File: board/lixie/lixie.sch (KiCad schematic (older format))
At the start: 27 parts

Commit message: got basic tokenizer working
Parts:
- added LS?: Speaker, symbol Speaker
- added R?: 10k, symbol R
- added R?: R, symbol R
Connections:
- net labels added: BOOT0, BTN_SLEEP, DBG_TCK, DBG_TMS, NRST, PIEZO
- wire segments 122 -> 131
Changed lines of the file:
@@
 	4900 9400 4600 9400
 Connection ~ 4600 9400
+Wire Wire Line
+	6250 9750 6600 9750
+Wire Wire Line
+	6250 9650 6600 9650
+Text Label 6600 9650 0    60   ~ 0
+DBG_TMS
+Text Label 6600 9750 0    60   ~ 0
+DBG_TCK
+Wire Wire Line
+	3650 9900 4900 9900
+Wire Wire Line
+	3650 10000 4900 10000
+Text Label 3650 9900 2    60   ~ 0
+NRST
+$Comp
+L R R?
+U 1 1 5E214C5B
+P 3850 10200
+F 0 "R?" V 3930 10200 50  0000 C CNN
+F 1 "10k" V 3850 10200 50  0000 C CNN
+F 2 "" V 3780 10200 50  0000 C CNN
+F 3 "" H 3850 10200 50  0000 C CNN
+	1    3850 10200
+	1    0    0    -1
+$EndComp
+Wire Wire Line
+	3850 10000 3850 10050
+Connection ~ 3850 10000
+$Comp
+L GND #PWR?
+U 1 1 5E21555C
+P 3850 10400
+F 0 "#PWR?" H 3850 10150 50  0001 C CNN
+F 1 "GND" H 3850 10250 50  0000 C CNN
+F 2 "" H 3850 10400 50  0001 C CNN
+F 3 "" H 3850 10400 50  0001 C CNN
+	1    3850 10400
+	1    0    0    -1
+$EndComp
+Wire Wire Line
+	3850 10350 3850 10400
+Text Label 3650 10000 2    60   ~ 0
+BOOT0
+Wire Wire Line
+	4900 11500 4600 11500
+Text Label 4600 11500 2    60   ~ 0
+BTN_SLEEP
+Wire Wire Line
+	3950 11400 4900 11400
+$Comp
+L Speaker LS?
+U 1 1 5E218279
+P 3550 11200
+F 0 "LS?" H 3600 11425 50  0000 R CNN
+F 1 "Speaker" H 3600 11350 50  0000 R CNN
+F 2 "" H 3550 11000 50  0000 C CNN
+F 3 "" H 3540 11150 50  0000 C CNN
+	1    3550 11200
+	0    -1   -1   0
+$EndComp
+$Comp
+L R R?
+U 1 1 5E218871
+P 3800 11400
+F 0 "R?" V 3880 11400 50  0000 C CNN
+F 1 "R" V 3800 11400 50  0000 C CNN
+F 2 "" V 3730 11400 50  0000 C CNN
+F 3 "" H 3800 11400 50  0000 C CNN
+	1    3800 11400
+	0    1    1    0
+$EndComp
+$Comp
+L GND #PWR?
+U 1 1 5E219525
+P 3550 11500
+F 0 "#PWR?" H 3550 11250 50  0001 C CNN
+F 1 "GND" H 3550 11350 50  0000 C CNN
+F 2 "" H 3550 11500 50  0001 C CNN
+F 3 "" H 3550 11500 50  0001 C CNN
+	1    3550 11500
+	1    0    0    -1
+$EndComp
+Wire Wire Line
+	3550 11400 3550 11500
+Text Label 4600 11400 2    60   ~ 0
+PIEZO
 $EndSCHEMATC

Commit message: made some footprints, fixed the power diode circuitry
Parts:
- removed Q?: Q_PJFET_DGS, symbol Q_PJFET_DGS
- removed R?: R, symbol R
- removed U?: LM66100, symbol LM66100
- added D?: D, symbol D
- added U?: MAX40200, symbol MAX40200
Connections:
- wire segments 131 -> 126
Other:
- note added: "3.3v Regulator"
- note added: "Ideal Diode"
- note added: "LED Matrix Driver"
- note added: "Main MCU"
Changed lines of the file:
@@
-$EndComp
-$Comp
-L LM66100 U?
-U 1 1 5E1F1034
-P 10450 9550
-F 0 "U?" H 10450 9600 60  0000 C CNN
-F 1 "LM66100" H 10450 9500 60  0000 C CNN
-F 2 "" H 10450 9400 60  0001 C CNN
-F 3 "" H 10450 9400 60  0001 C CNN
-	1    10450 9550
-	1    0    0    -1
 $EndComp
 $Comp
@@
 $EndComp
 $Comp
-L Q_PJFET_DGS Q?
-U 1 1 5E1F2946
-P 10450 10300
-F 0 "Q?" H 10650 10350 50  0000 L CNN
-F 1 "Q_PJFET_DGS" H 10650 10250 50  0000 L CNN
-F 2 "" H 10650 10400 50  0000 C CNN
-F 3 "" H 10450 10300 50  0000 C CNN
-	1    10450 10300
-	0    1    1    0
-$EndComp
-$Comp
-L R R?
-U 1 1 5E1F363E
-P 11400 9950
-F 0 "R?" V 11480 9950 50  0000 C CNN
-F 1 "R" V 11400 9950 50  0000 C CNN
-F 2 "" V 11330 9950 50  0000 C CNN
-F 3 "" H 11400 9950 50  0000 C CNN
-	1    11400 9950
-	1    0    0    -1
-$EndComp
-$Comp
-L +BATT #PWR?
-U 1 1 5E1F37C6
-P 11400 9750
-F 0 "#PWR?" H 11400 9600 50  0001 C CNN
-F 1 "+BATT" H 11400 9890 50  0000 C CNN
-F 2 "" H 11400 9750 50  0001 C CNN
-F 3 "" H 11400 9750 50  0001 C CNN
-	1    11400 9750
-	1    0    0    -1
-$EndComp
-$Comp
 L LED_ARGB D?
 U 1 1 5E1FE9E8
@@
 Connection ~ 6650 6250
 Wire Wire Line
-	9500 9300 9500 9200
-Wire Wire Line
-	11750 9100 11750 10400
-Wire Wire Line
-	11400 9750 11400 9800
-Connection ~ 11250 10100
+	9500 9200 9500 9550
 Connection ~ 11750 9300
 Wire Wire Line
-	11750 10400 10650 10400
-Connection ~ 9500 10100
-Wire Wire Line
-	10250 10100 9500 10100
-Wire Wire Line
-	10250 10100 10250 10400
-Wire Wire Line
-	10450 10100 11400 10100
-Wire Wire Line
-	11250 9550 11250 10100
-Wire Wire Line
-	11150 9550 11250 9550
-Wire Wire Line
 	9500 9550 9750 9550
-Wire Wire Line
-	9500 10300 9500 9550
 Wire Wire Line
 	9650 9800 9650 9850
@@
 Text Label 4600 11400 2    60   ~ 0
 PIEZO
+$Comp
+L MAX40200 U?
+U 1 1 5E374A62
+P 10450 9550
+F 0 "U?" H 10450 9600 60  0000 C CNN
+F 1 "MAX40200" H 10450 9500 60  0000 C CNN
+F 2 "" H 10450 9400 60  0001 C CNN
+F 3 "" H 10450 9400 60  0001 C CNN
+	1    10450 9550
+	1    0    0    -1
+$EndComp
+Wire Wire Line
+	9500 10100 9500 10300
+Connection ~ 9500 9300
+Wire Wire Line
+	11750 10100 11750 9300
+$Comp
+L D D?
+U 1 1 5E37A215
+P 10450 10100
+F 0 "D?" H 10450 10200 50  0000 C CNN
+F 1 "D" H 10450 10000 50  0000 C CNN
+F 2 "" H 10450 10100 50  0000 C CNN
+F 3 "" H 10450 10100 50  0000 C CNN
+	1    10450 10100
+	-1   0    0    1
+$EndComp
+Wire Wire Line
+	9500 10100 10300 10100
+Wire Wire Line
+	10600 10100 11750 10100
+Text Notes 10200 9150 0    60   ~ 0
+Ideal Diode
+Text Notes 12550 9150 0    60   ~ 0
+3.3v Regulator
+Text Notes 4700 3800 0    60   ~ 0
+LED Matrix Driver
+Text Notes 5350 8200 0    60   ~ 0
+Main MCU
 $EndSCHEMATC

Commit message: started working on layout
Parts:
- removed P?: USB_A, symbol USB_A
- added P1: USB_OTG, lixie:USB_Micro-B_Molex-105017-0001, symbol USB_OTG
- BT1: renamed from BT?; footprint (none) -> Pin_Headers:Pin_Header_Straight_1x02
- D1, D10, D11, D12, D13, D14, D15, D16, D2, D3, D4, D5, D6, D7, D8, D9: renamed from D?; footprint (none) -> lixie:LED_ARGB_0606
- D17: renamed from D?; footprint (none) -> Diodes_SMD:SOD-123
- LS1: renamed from LS?; footprint (none) -> lixie:PKMCS0909E4000-R1
- R1, R2, R3, R4, R5: renamed from R?; footprint (none) -> Resistors_SMD:R_0805_HandSoldering
- U1: renamed from U?; footprint (none) -> lixie:IS31FL3738
- U2: renamed from U?; footprint (none) -> lixie:MIC550x
- U3: renamed from U?; footprint (none) -> lixie:MAX40200
- U4: renamed from U?; footprint (none) -> lixie:STM32L073RZT3

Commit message: started working on layout
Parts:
- removed LS1: Speaker, lixie:PKMCS0909E4000-R1, symbol Speaker
- removed R5: R, Resistors_SMD:R_0805_HandSoldering, symbol R
- added P?: CONN_01X04, symbol CONN_01X04
- added SW?: SW_Push, symbol SW_Push
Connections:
- net labels added: SWCLK, SWDIO
- net labels removed: DBG_TCK, DBG_TMS, PIEZO
- wire segments 126 -> 132
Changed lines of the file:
@@
 LIBS:lixie
 LIBS:frkbmb28-cache
+LIBS:Switch
 LIBS:lixie-cache
 EELAYER 25 0
@@
 Connection ~ 4600 9400
 Wire Wire Line
-	6250 9750 6600 9750
-Wire Wire Line
-	6250 9650 6600 9650
+	6250 9750 7750 9750
+Wire Wire Line
+	6250 9650 7750 9650
 Text Label 6600 9650 0    60   ~ 0
-DBG_TMS
+SWDIO
 Text Label 6600 9750 0    60   ~ 0
-DBG_TCK
+SWCLK
 Wire Wire Line
 	3650 9900 4900 9900
@@
 BOOT0
 Wire Wire Line
-	4900 11500 4600 11500
-Text Label 4600 11500 2    60   ~ 0
+	4750 11650 4450 11650
+Text Label 4500 11850 2    60   ~ 0
 BTN_SLEEP
-Wire Wire Line
-	3950 11400 4900 11400
-$Comp
-L Speaker LS1
-U 1 1 5E218279
-P 3550 11200
-F 0 "LS1" H 3600 11425 50  0000 R CNN
-F 1 "Speaker" H 3600 11350 50  0000 R CNN
-F 2 "lixie:PKMCS0909E4000-R1" H 3550 11000 50  0001 C CNN
-F 3 "" H 3540 11150 50  0000 C CNN
-	1    3550 11200
-	0    -1   -1   0
-$EndComp
-$Comp
-L R R5
-U 1 1 5E218871
-P 3800 11400
-F 0 "R5" V 3880 11400 50  0000 C CNN
-F 1 "R" V 3800 11400 50  0000 C CNN
-F 2 "Resistors_SMD:R_0805_HandSoldering" V 3730 11400 50  0001 C CNN
-F 3 "" H 3800 11400 50  0000 C CNN
-	1    3800 11400
-	0    1    1    0
-$EndComp
-$Comp
-L GND #PWR021
-U 1 1 5E219525
-P 3550 11500
-F 0 "#PWR021" H 3550 11250 50  0001 C CNN
-F 1 "GND" H 3550 11350 50  0000 C CNN
-F 2 "" H 3550 11500 50  0001 C CNN
-F 3 "" H 3550 11500 50  0001 C CNN
-	1    3550 11500
-	1    0    0    -1
-$EndComp
-Wire Wire Line
-	3550 11400 3550 11500
-Text Label 4600 11400 2    60   ~ 0
-PIEZO
 $Comp
 L MAX40200 U3
@@
 	0    -1   -1   0
 $EndComp
+$Comp
+L SW_Push SW?
+U 1 1 5E3808C7
+P 4250 11650
+F 0 "SW?" H 4300 11750 50  0000 L CNN
+F 1 "SW_Push" H 4250 11590 50  0000 C CNN
+F 2 "" H 4250 11850 50  0001 C CNN
+F 3 "" H 4250 11850 50  0001 C CNN
+	1    4250 11650
+	1    0    0    -1
+$EndComp
+Wire Wire Line
+	4900 11500 4750 11500
+Wire Wire Line
+	4750 11500 4750 11650
+$Comp
+L GND #PWR023
+U 1 1 5E38221E
+P 3950 11750
+F 0 "#PWR023" H 3950 11500 50  0001 C CNN
+F 1 "GND" H 3950 11600 50  0000 C CNN
+F 2 "" H 3950 11750 50  0001 C CNN
+F 3 "" H 3950 11750 50  0001 C CNN
+	1    3950 11750
+	1    0    0    -1
+$EndComp
+Wire Wire Line
+	4050 11650 3950 11650
+Wire Wire Line
+	3950 11650 3950 11750
+$Comp
+L CONN_01X04 P?
+U 1 1 5E382C34
+P 7950 9600
+F 0 "P?" H 7950 9850 50  0000 C CNN
+F 1 "CONN_01X04" V 8050 9600 50  0000 C CNN
+F 2 "" H 7950 9600 50  0000 C CNN
+F 3 "" H 7950 9600 50  0000 C CNN
+	1    7950 9600
+	1    0    0    -1
+$EndComp
+Wire Wire Line
+	7750 9550 7250 9550
+$Comp
+L +5V #PWR024
+U 1 1 5E38635F
+P 7400 9400
+F 0 "#PWR024" H 7400 9250 50  0001 C CNN
+F 1 "+5V" H 7400 9540 50  0000 C CNN
+F 2 "" H 7400 9400 50  0001 C CNN
+F 3 "" H 7400 9400 50  0001 C CNN
+	1    7400 9400
+	1    0    0    -1
+$EndComp
+$Comp
+L GND #PWR025
+U 1 1 5E386C59
+P 7250 9500
+F 0 "#PWR025" H 7250 9250 50  0001 C CNN
+F 1 "GND" H 7250 9350 50  0000 C CNN
+F 2 "" H 7250 9500 50  0001 C CNN
+F 3 "" H 7250 9500 50  0001 C CNN
+	1    7250 9500
+	-1   0    0    1
+$EndComp
+Wire Wire Line
+	7250 9550 7250 9500
+Wire Wire Line
+	7750 9450 7400 9450
+Wire Wire Line
+	7400 9450 7400 9400
 $EndSCHEMATC

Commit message: laid out the board
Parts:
- removed D1, D10, D11, D12, D13, D14, D15, D16, D2, D3, D4, D5, D6, D7, D8, D9: LED_ARGB, lixie:LED_ARGB_0606, symbol LED_ARGB
- added D1, D10, D11, D12, D13, D14, D15, D16, D2, D3, D4, D5, D6, D7, D8, D9: LED_RGAB, lixie:LED_RGAB_0606, symbol LED_RGAB
- added F1, F2, F3: Polyfuse, Resistors_SMD:R_1206_HandSoldering, symbol Polyfuse
- added R5, R6: 4.7k, Resistors_SMD:R_0805_HandSoldering, symbol R
- P2: renamed from P?; footprint (none) -> Pin_Headers:Pin_Header_Straight_1x04
- SW1: renamed from SW?; footprint (none) -> Buttons_Switches_SMD:SW_SPST_TL3342
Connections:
- net labels added: LED_CURRENT
- wire segments 132 -> 141
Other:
- moved on the sheet: BT1

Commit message: added some test points
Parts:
- added SCL_TST1, SDA_TST1, USB_DM_TST1, USB_DP_GND1, USB_DP_GND2, USB_DP_TST1, VBUS_TST1: TestPoint, Connector_PinHeader_2.54mm:PinHeader_1x01_P2.54mm_Vertical, symbol Connector:TestPoint
- BT1: symbol Battery_Cell -> lixie-rescue:Battery_Cell
- D1, D10, D11, D12, D13, D14, D15, D16, D2, D3, D4, D5, D6, D7, D8, D9: symbol LED_RGAB -> lixie-rescue:LED_RGAB
- D17: symbol D -> lixie-rescue:D
- F1, F2, F3: symbol Polyfuse -> lixie-rescue:Polyfuse
- P1: symbol USB_OTG -> lixie-rescue:USB_OTG
- P2: symbol CONN_01X04 -> lixie-rescue:CONN_01X04
- R1, R2, R3, R4, R5, R6: symbol R -> lixie-rescue:R
- SW1: symbol SW_Push -> lixie-rescue:SW_Push
- U1: symbol IS31FL3738 -> lixie-rescue:IS31FL3738
- U2: symbol MIC550x -> lixie-rescue:MIC550x
- U3: symbol MAX40200 -> lixie-rescue:MAX40200
- U4: symbol STM32L073xZ -> lixie-rescue:STM32L073xZ
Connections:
- net GND: now also USB_DP_GND1.1, USB_DP_GND2.1
- net SCL: now also SCL_TST1.1
- net SDA: now also SDA_TST1.1
- net USB_DM: now also USB_DM_TST1.1
- net USB_DP: now also USB_DP_TST1.1
- net VBUS: now also VBUS_TST1.1
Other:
- moved on the sheet: BT1, D17, F1, F2, F3, P1, P2, R4, R5, R6, SW1, U2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

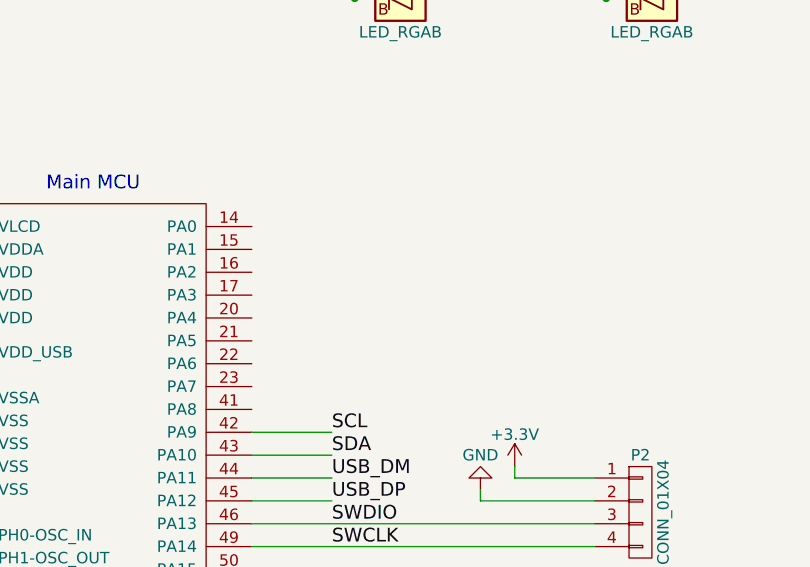
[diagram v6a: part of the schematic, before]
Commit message: apparently I routed EVERY FUCKING LED WRONG so now I gotta fix it
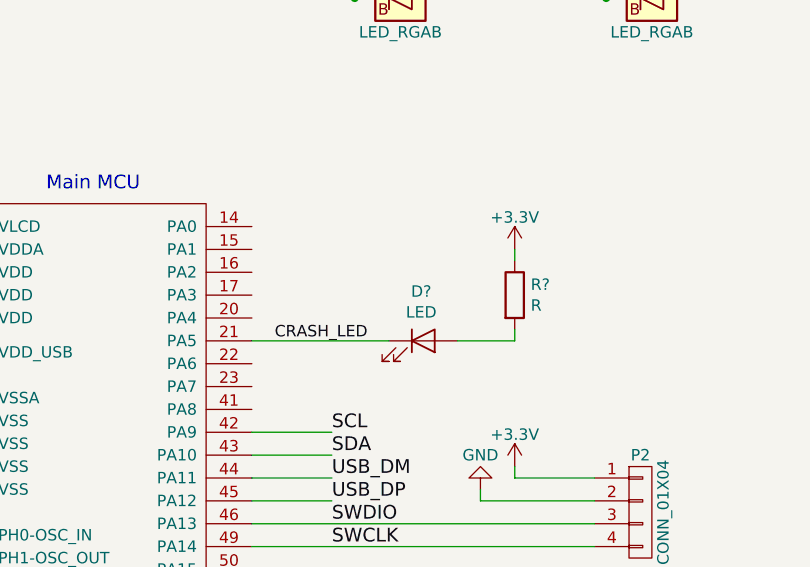
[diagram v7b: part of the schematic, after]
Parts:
- added D?: LED, symbol Device:LED
- added R?: R, symbol Device:R
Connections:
- net +3V3: now also R?.1
- net CRASH_LED: now reaches U4.21 (PA5)
- net CRASH_LED: now also D?.1 (K)
- new net: D?.2 (A), R?.2
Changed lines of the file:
@@
 Wire Wire Line
 	11350 8900 11800 8900
+Text Label 5900 8850 0    50   ~ 0
+CRASH_LED
+$Comp
+L Device:LED D?
+U 1 1 5E4BD99C
+P 6550 8850
+F 0 "D?" H 6541 9066 50  0000 C CNN
+F 1 "LED" H 6541 8975 50  0000 C CNN
+F 2 "" H 6550 8850 50  0001 C CNN
+F 3 "~" H 6550 8850 50  0001 C CNN
+	1    6550 8850
+	1    0    0    -1
+$EndComp
+Wire Wire Line
+	6700 8850 6950 8850
+$Comp
+L Device:R R?
+U 1 1 5E4E9293
+P 6950 8650
+F 0 "R?" H 7020 8696 50  0000 L CNN
+F 1 "R" H 7020 8605 50  0000 L CNN
+F 2 "" V 6880 8650 50  0001 C CNN
+F 3 "~" H 6950 8650 50  0001 C CNN
+	1    6950 8650
+	1    0    0    -1
+$EndComp
+$Comp
+L lixie-rescue:+3.3V #PWR?
+U 1 1 5E4EA8C3
+P 6950 8450
+F 0 "#PWR?" H 6950 8300 50  0001 C CNN
+F 1 "+3.3V" H 6950 8590 50  0000 C CNN
+F 2 "" H 6950 8450 50  0001 C CNN
+F 3 "" H 6950 8450 50  0001 C CNN
+	1    6950 8450
+	1    0    0    -1
+$EndComp
+Wire Wire Line
+	6950 8450 6950 8500
+Wire Wire Line
+	6950 8800 6950 8850
+Wire Wire Line
+	5800 8850 6400 8850
 $EndSCHEMATC

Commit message: kicad crashed so now I am wiring the LEDs for a fucking 3rd time
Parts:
- removed D1, D10, D11, D12, D13, D14, D15, D16, D2, D3, D4, D5, D6, D7, D8, D9: LED_RGAB, lixie:LED_RGAB_0606, symbol lixie-rescue:LED_RGAB
- added D1, D10, D11, D12, D13, D14, D15, D16, D2, D3, D4, D5, D6, D7, D8, D9: LED_ARBG, lixie:LED_LSTD_0606, symbol lixie-rescue:LED_ARBG
- added JP1: Jumper_2_Open, Jumper:SolderJumper-2_P1.3mm_Open_TrianglePad1.0x1.5mm, symbol Jumper:Jumper_2_Open
- D17: footprint Diodes_SMD:SOD-123 -> Diode_SMD:D_SOD-123
- D18: renamed from D?; footprint (none) -> LED_SMD:LED_0805_2012Metric_Pad1.15x1.40mm_HandSolder
- F1, F2, F3: footprint Resistors_SMD:R_1206_HandSoldering -> Fuse:Fuse_0805_2012Metric_Pad1.15x1.40mm_HandSolder
- R1: renamed from R5; footprint Resistors_SMD:R_0805_HandSoldering -> Resistor_SMD:R_0805_2012Metric_Pad1.15x1.40mm_HandSolder
- R2: renamed from R6; footprint Resistors_SMD:R_0805_HandSoldering -> Resistor_SMD:R_0805_2012Metric_Pad1.15x1.40mm_HandSolder
- R3: renamed from R1; footprint Resistors_SMD:R_0805_HandSoldering -> Resistor_SMD:R_0805_2012Metric_Pad1.15x1.40mm_HandSolder
- R4: renamed from R2; footprint Resistors_SMD:R_0805_HandSoldering -> Resistor_SMD:R_0805_2012Metric_Pad1.15x1.40mm_HandSolder
- R5: renamed from R3; footprint Resistors_SMD:R_0805_HandSoldering -> Resistor_SMD:R_0805_2012Metric_Pad1.15x1.40mm_HandSolder
- R6: renamed from R?; footprint (none) -> Resistor_SMD:R_0805_2012Metric_Pad1.15x1.40mm_HandSolder
- R7: renamed from R4; footprint Resistors_SMD:R_0805_HandSoldering -> Resistor_SMD:R_0805_2012Metric_Pad1.15x1.40mm_HandSolder
- renumbered U3 to U2, U2 to U3
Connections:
- net GND: now also JP1.1 (A)
- net NRST: now also JP1.2 (B)
- net VBUS: no longer VBUS_TST1.1
- net at U1.10 (CS1): now also D1.1 (A), D9.1 (A)
- net at U1.11 (CS2): now also D10.1 (A), D2.1 (A)
- net at U1.13 (CS3): now also D11.1 (A), D3.1 (A)
- net at U1.14 (CS4): now also D12.1 (A), D4.1 (A)
- net at U1.15 (CS5): now also D13.1 (A), D5.1 (A)
- net at U1.16 (CS6): now also D14.1 (A), D6.1 (A)
- net at U1.18 (CS7): now also D15.1 (A), D7.1 (A)
- net at U1.19 (CS8): now also D16.1 (A), D8.1 (A)
- net at U1.2 (SW1): now also D10.3 (BK), D11.3 (BK), D12.3 (BK), D13.3 (BK), D14.3 (BK), D15.3 (BK), D16.3 (BK), D9.3 (BK)
- net at U1.3 (SW2): now also D10.4 (GK), D11.4 (GK), D12.4 (GK), D13.4 (GK), D14.4 (GK), D15.4 (GK), D16.4 (GK), D9.4 (GK)
- net at U1.5 (SW3): now also D10.2 (RK), D11.2 (RK), D12.2 (RK), D13.2 (RK), D14.2 (RK), D15.2 (RK), D16.2 (RK), D9.2 (RK)
- net at U1.6 (SW4): now also D1.3 (BK), D2.3 (BK), D3.3 (BK), D4.3 (BK), D5.3 (BK), D6.3 (BK), D7.3 (BK), D8.3 (BK)
- net at U1.7 (SW5): now also D1.4 (GK), D2.4 (GK), D3.4 (GK), D4.4 (GK), D5.4 (GK), D6.4 (GK), D7.4 (GK), D8.4 (GK)
- net at U1.9 (SW6): now also D1.2 (RK), D2.2 (RK), D3.2 (RK), D4.2 (RK), D5.2 (RK), D6.2 (RK), D7.2 (RK), D8.2 (RK)
- net at D17.1 (K), F2.2, U2.5 (VOUT): now also VBUS_TST1.1
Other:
- moved on the sheet: BT1, D17, D18, F1, F2, F3, P1, P2, R6, R7, SW1, U2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
